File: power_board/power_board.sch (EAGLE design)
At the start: 33 parts, among them J5 20021311-00010T4LF, J6 20021311-00010T4LF, J7 20021311-00010T4LF, Q2 NPN, Q3 600mA/40V, Q4 NTMD4184PFR2G, U1 DRV8871, U11 INA219AIDCNR

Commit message: Added 3D models for power board
- All components now have proper 3D models added to it
- Full 3D step file of the board now available (also in Fusion360)
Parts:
- removed Q2: NPN, SparkFun-DiscreteSemi:TRANSISTOR_NPNMMBT5088
- added Q1: 600mA/40V, SparkFun-DiscreteSemi:TRANS_NPN-MMBT2222AL
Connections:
- net GND: now also Q1.E; no longer Q2.E
- net GND0: now also Q1.C; no longer Q2.C
- net N$7: now also Q1.B; no longer Q2.B

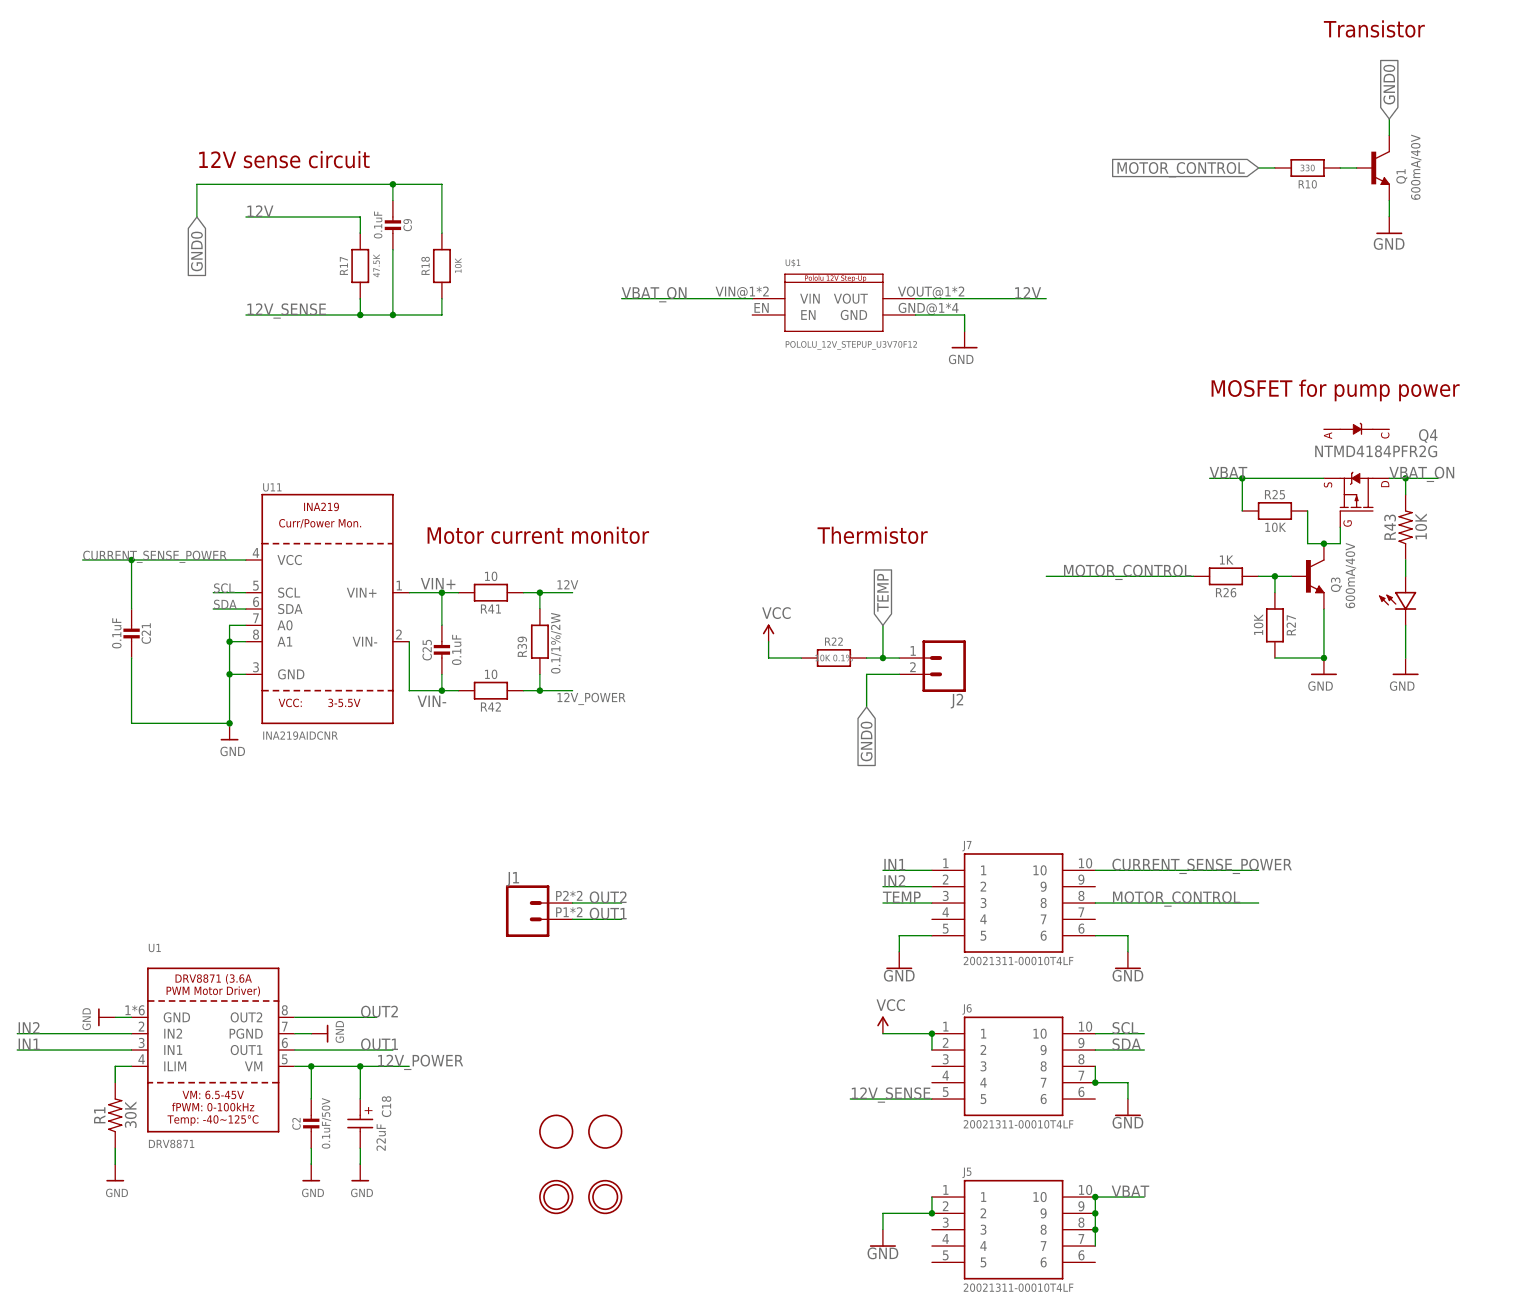
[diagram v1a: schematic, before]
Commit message: v0.2 - power board update
- replaced DRV8871 driver with PCA9685 driver
- added more caps
- replaced 2-pin poke home with 3-pin 2.54mm header
- rerouted many traces and vias
- moved some components around
- added schematic
- updated render, gerber
- ERC/DRC
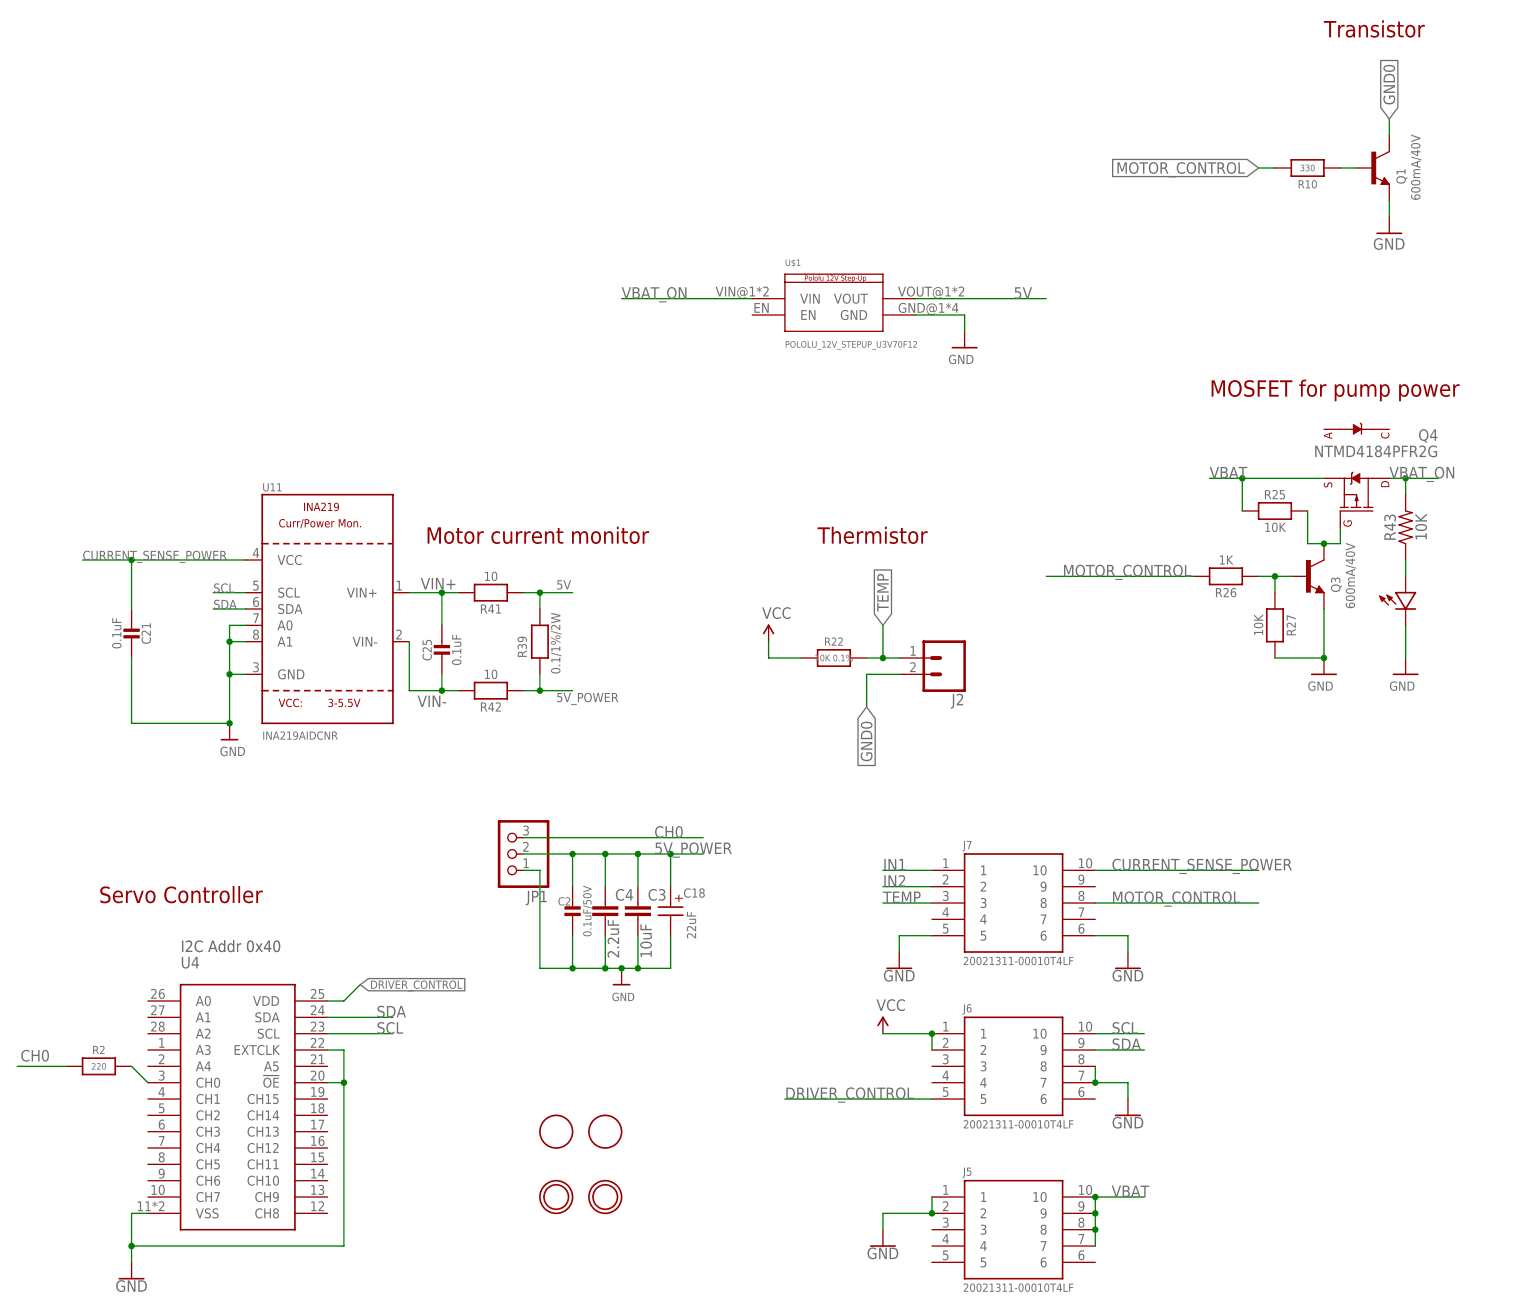
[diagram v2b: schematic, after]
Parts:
- removed C9: 0.1uF, Adafruit Feather 32u4 Bluefruit LE:MICROBUILDER_CAP_CERAMIC_0402MP
- removed J1: (no value), SparkFun-Connectors:CONN_02SMALL_POKEHOME
- removed R1: 30K, SparkFun-Resistors:RESISTOR0805
- removed R17: 47.5K, Adafruit Feather 32u4 Bluefruit LE:MICROBUILDER_RESISTOR_0402MP
- removed R18: 10K, Adafruit Feather 32u4 Bluefruit LE:MICROBUILDER_RESISTOR_0402MP
- removed U1: DRV8871, microbuilder:DRV8871
- added C3: 10uF, SparkFun-Passives:CAP0805
- added C4: 2.2uF, SparkFun-Passives:CAP1206
- added JP1: (no value), adafruit:PINHD-1X3
- added R2: 220, Adafruit Feather 32u4 Bluefruit LE:MICROBUILDER_RESISTOR_0402MP
- added U4: (no value), PCA9685:PCA9685HVQFN28
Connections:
- removed net 12V: R17.2, R39.2, R41.1, U$1.VOUT
- removed net 12V_POWER: C18.+, C2.1, R39.1, R42.1, U1.VM
- removed net 12V_SENSE: C9.1, J6.5, R17.1, R18.1
- removed net N$2: R1.2, U1.ILIM
- removed net OUT1: J1.1, U1.OUT1
- removed net OUT2: J1.2, U1.OUT2
- new net 5V: R39.2, R41.1, U$1.VOUT
- new net 5V_POWER: C18.+, C2.1, C3.1, C4.1, JP1.2, R39.1, R42.1
- new net CH0: JP1.3, R2.1
- new net DRIVER_CONTROL: J6.5, U4.VDD
- new net N$9: R2.2, U4.CH0
- net GND: now also C3.2, C4.2, JP1.1, U4.!OE, U4.EXTCLK, U4.VSS; no longer R1.1, U1.GND, U1.PGND
- net GND0: no longer C9.2, R18.2
- net IN1: no longer U1.IN1
- net IN2: no longer U1.IN2
- net SCL: now also U4.SCL
- net SDA: now also U4.SDA
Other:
- note added: "I2C Addr 0x40"
- note added: "Servo Controller"
- note removed: "12V sense circuit"
- moved on the sheet: C18, C2

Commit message: v0.3 - power board update
- design update
- replaced U3V70x with U1V11x step up voltage regulator. This steps up from batt. voltage (~4V) to 5V from as low as 0.5V. This allows servo to work even with large voltage drops
- Added extra caps on input and output of voltage reg.
- Increased cutout for servo cable to go outside the board dimension. Allows more room for wire to bend
- pushed servo cable header pins further in the board to allow room for large connector head
- moved traces and components around to accomodate new design
- silkscreen, dimensions, board outline (dxf), gerbers, render & schematic update
- 3D step file still not updated
- ERC/DRC
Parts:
- removed U$1: POLOLU_12V_STEPUP_U3V70F12, Pololu U3V70x Step Up:POLOLU_12V_STEPUP_U3V70F12
- added C1: 2.2uF, SparkFun-Passives:CAP1206
- added C5, C6: 10uF, SparkFun-Passives:CAP1206
- added U5: POLOLU_STEPUP_U1V11X, Pololu Step Up Vregs:POLOLU_STEPUP_U1V11X
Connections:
- removed net IN1: J7.1
- removed net IN2: J7.2
- net 5V: now also U5.VOUT; no longer U$1.VOUT
- net 5V_POWER: now also C1.1
- net GND: now also C1.2, C5.2, C6.2, U5.GND; no longer U$1.GND
- net VBAT_ON: now also C5.1, C6.1, U5.VIN; no longer U$1.VIN
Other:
- moved on the sheet: C18, C3

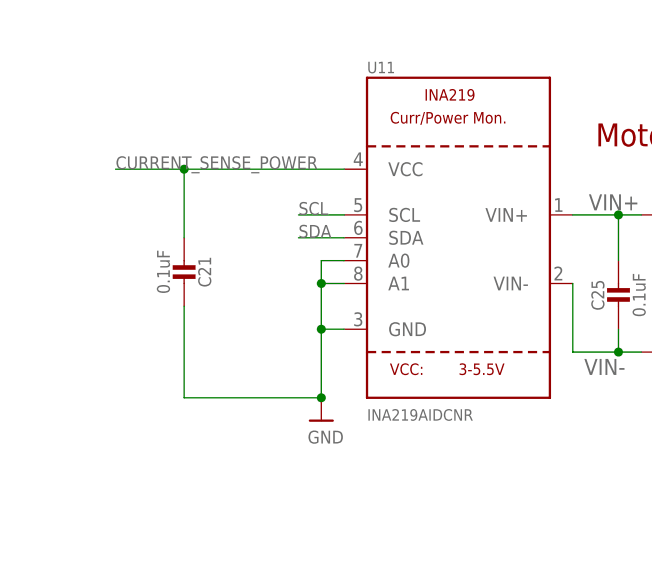
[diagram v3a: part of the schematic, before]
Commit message: v0.4 - power board update
- INA219 I2C address now changed from 0x40 to 0x44 to avoid conflict with PCA9685 (added pull-up resistor on pin A0)
- gerber files updated
- everything else functionally the same
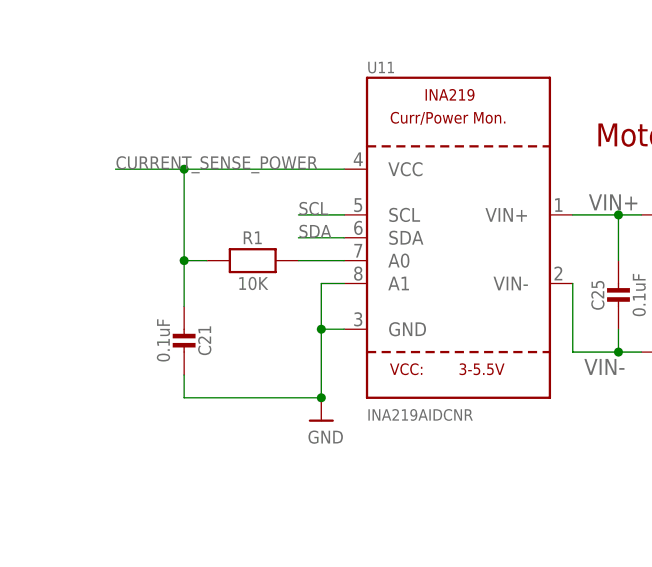
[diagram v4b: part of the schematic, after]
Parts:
- added R1: 10K, Adafruit Feather 32u4 Bluefruit LE:MICROBUILDER_RESISTOR_0402MP
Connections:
- new net N$1: R1.2, U11.A0
- net CURRENT_SENSE_POWER: now also R1.1
- net GND: no longer U11.A0
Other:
- moved on the sheet: C21
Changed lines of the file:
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@@
 <part name="C6" library="SparkFun-Passives" deviceset="CAP" device="1206" value="10uF"/>
 <part name="GND5" library="SparkFun-Aesthetics" deviceset="GND" device=""/>
+<part name="R1" library="Adafruit Feather 32u4 Bluefruit LE" deviceset="MICROBUILDER_RESISTOR" device="_0402MP" override_package3d_urn="urn:adsk.eagle:package:24880645/2" override_package_urn="urn:adsk.eagle:footprint:24880646/1" value="10K">
+<attribute name="MPN" value="RC0402FR-7W10KL"/>
+</part>
 </parts>
 <sheets>
@@
 <attribute name="MPN" x="149.86" y="71.12" size="1.4224" layer="96" rot="R90" display="off"/>
 </instance>
-<instance part="C21" gate="G$1" x="86.36" y="73.66" smashed="yes" rot="R180">
-<attribute name="MPN" x="86.36" y="73.66" size="1.778" layer="96" rot="R180" display="off"/>
-<attribute name="NAME" x="88.65" y="72.41" size="1.4224" layer="95" rot="R270" align="center"/>
-<attribute name="VALUE" x="84.06" y="72.41" size="1.4224" layer="96" rot="R270" align="center"/>
+<instance part="C21" gate="G$1" x="86.36" y="66.04" smashed="yes" rot="R180">
+<attribute name="MPN" x="86.36" y="66.04" size="1.778" layer="96" rot="R180" display="off"/>
+<attribute name="NAME" x="88.65" y="64.79" size="1.4224" layer="95" rot="R270" align="center"/>
+<attribute name="VALUE" x="84.06" y="64.79" size="1.4224" layer="96" rot="R270" align="center"/>
 </instance>
 <instance part="C25" gate="G$1" x="134.62" y="68.58" smashed="yes">
@@
 <instance part="GND5" gate="1" x="170.18" y="111.76" smashed="yes">
 <attribute name="VALUE" x="167.64" y="109.22" size="1.4224" layer="96"/>
+</instance>
+<instance part="R1" gate="G$1" x="93.98" y="73.66" smashed="yes">
+<attribute name="MPN" x="93.98" y="73.66" size="1.778" layer="96" display="off"/>
+<attribute name="NAME" x="93.98" y="76.2" size="1.4224" layer="95" align="center"/>
+<attribute name="VALUE" x="93.98" y="71.12" size="1.4224" layer="96" ratio="15" align="center"/>
 </instance>
 </instances>
@@
 <pinref part="U11" gate="G$1" pin="GND"/>
 <pinref part="U$6" gate="G$1" pin="GND"/>
-<pinref part="U11" gate="G$1" pin="A0"/>
-<wire x1="104.14" y1="73.66" x2="101.6" y2="73.66" width="0.1524" layer="91"/>
-<wire x1="101.6" y1="73.66" x2="101.6" y2="71.12" width="0.1524" layer="91"/>
 <junction x="101.6" y="66.04"/>
 <pinref part="U11" gate="G$1" pin="A1"/>
 <wire x1="101.6" y1="71.12" x2="101.6" y2="66.04" width="0.1524" layer="91"/>
 <wire x1="104.14" y1="71.12" x2="101.6" y2="71.12" width="0.1524" layer="91"/>
-<junction x="101.6" y="71.12"/>
 <pinref part="C21" gate="G$1" pin="1"/>
-<wire x1="86.36" y1="68.58" x2="86.36" y2="58.42" width="0.1524" layer="91"/>
+<wire x1="86.36" y1="60.96" x2="86.36" y2="58.42" width="0.1524" layer="91"/>
 <wire x1="86.36" y1="58.42" x2="101.6" y2="58.42" width="0.1524" layer="91"/>
 <junction x="101.6" y="58.42"/>
@@
 <pinref part="C21" gate="G$1" pin="2"/>
 <wire x1="86.36" y1="83.82" x2="78.74" y2="83.82" width="0.1524" layer="91"/>
-<wire x1="86.36" y1="76.2" x2="86.36" y2="83.82" width="0.1524" layer="91"/>
+<wire x1="86.36" y1="68.58" x2="86.36" y2="73.66" width="0.1524" layer="91"/>
 <junction x="86.36" y="83.82"/>
+<pinref part="R1" gate="G$1" pin="1"/>
+<wire x1="86.36" y1="73.66" x2="86.36" y2="83.82" width="0.1524" layer="91"/>
+<wire x1="88.9" y1="73.66" x2="86.36" y2="73.66" width="0.1524" layer="91"/>
+<junction x="86.36" y="73.66"/>
 </segment>
 </net>
@@
 </segment>
 </net>
+<net name="N$1" class="1">
+<segment>
+<pinref part="U11" gate="G$1" pin="A0"/>
+<pinref part="R1" gate="G$1" pin="2"/>
+<wire x1="104.14" y1="73.66" x2="99.06" y2="73.66" width="0.1524" layer="91"/>
+</segment>
+</net>
